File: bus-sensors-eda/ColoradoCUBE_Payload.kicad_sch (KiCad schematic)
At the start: 32 parts, among them J5 Conn_01x02, J6 Conn_01x02, J7 Conn_01x02, SW1 SW_SPST, U1 PIC18F27Q84-E/SP

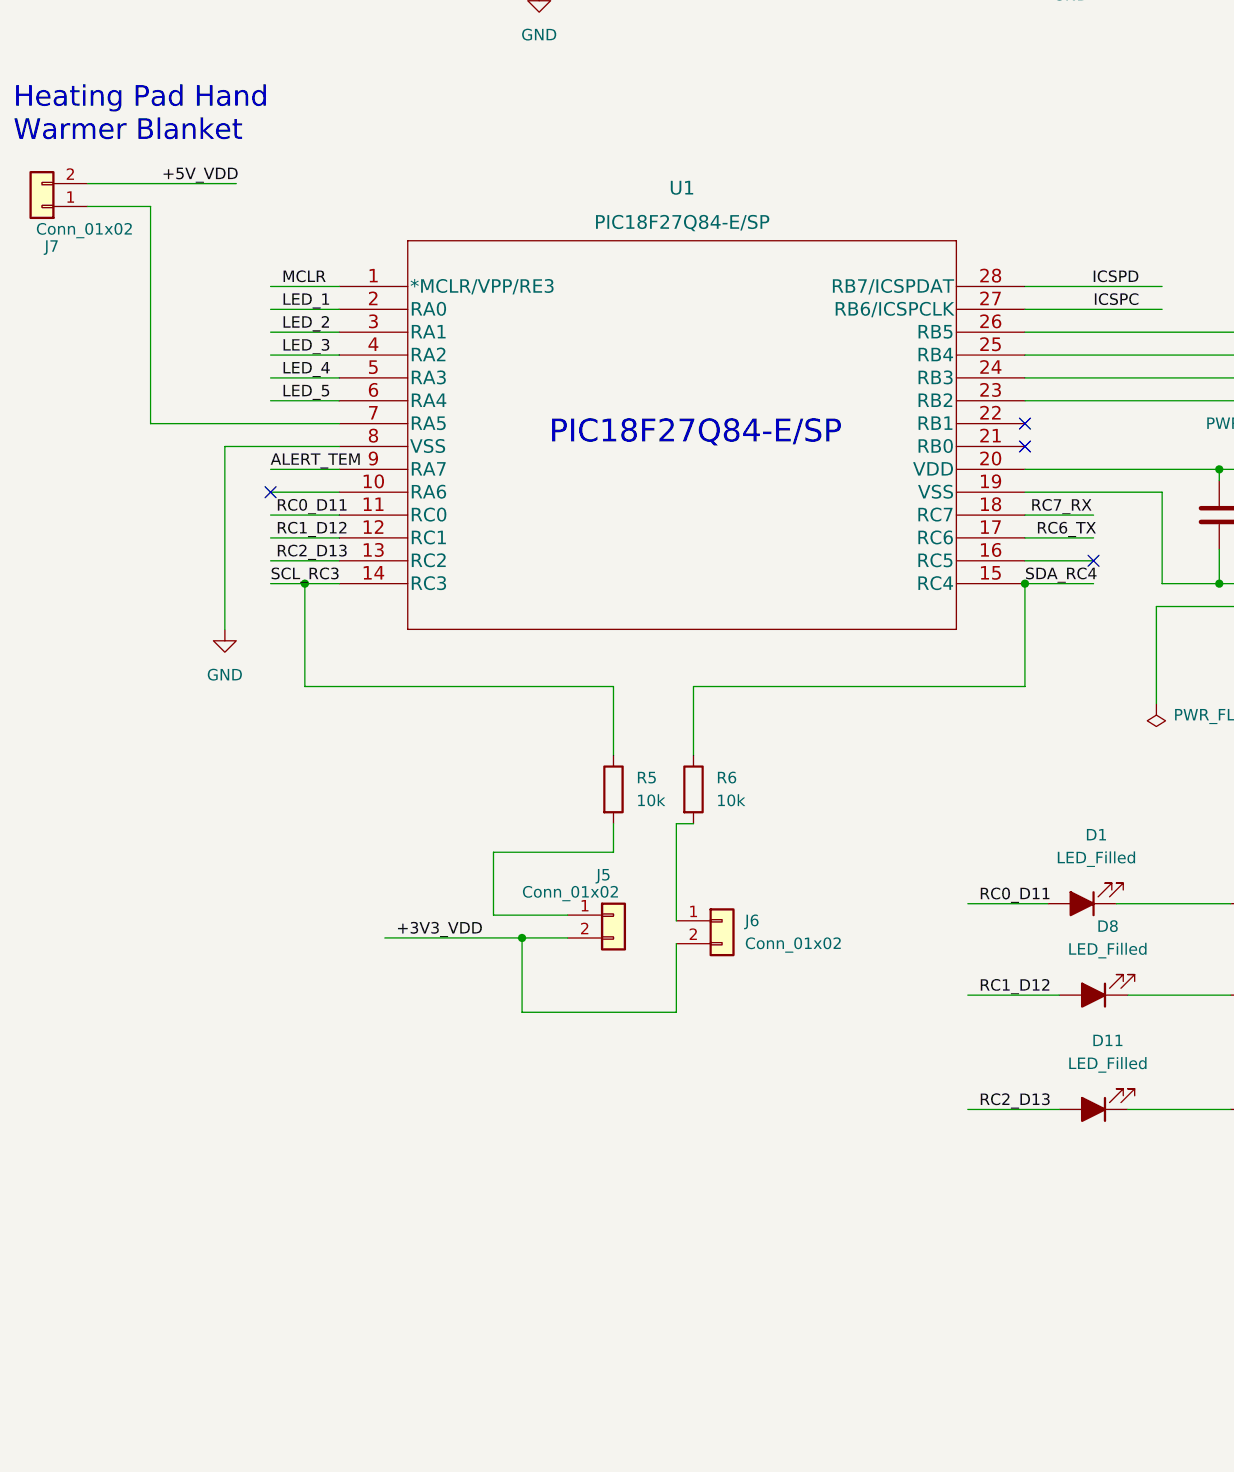
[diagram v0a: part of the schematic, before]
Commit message: moving files under eda dir
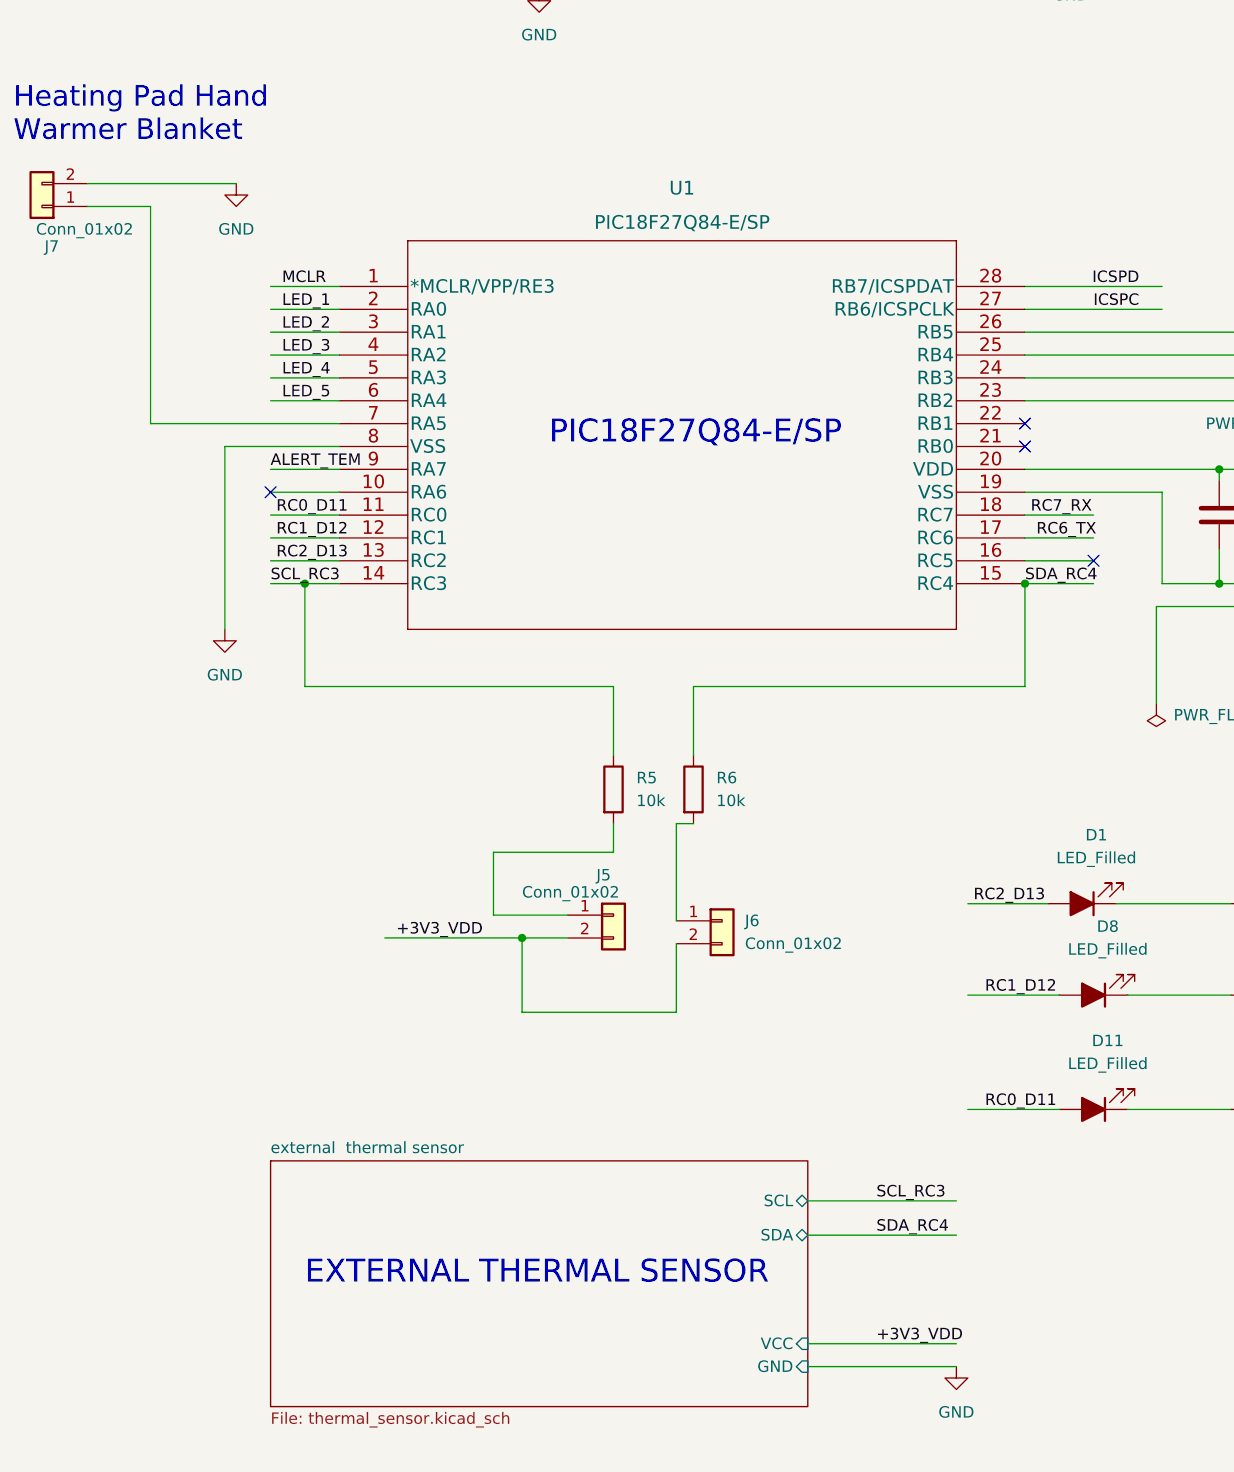
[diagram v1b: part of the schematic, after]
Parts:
- D1, D11, D8: footprint LED_SMD:LED_2512_6332Metric_Pad1.52x3.35mm_HandSolder -> LED_SMD:LED_2010_5025Metric_Pad1.52x2.65mm_HandSolder
- D10, D9: footprint LED_SMD:LED_1210_3225Metric_Pad1.42x2.65mm_HandSolder -> LED_SMD:LED_2010_5025Metric_Pad1.52x2.65mm_HandSolder
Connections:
- net +5V_VDD: no longer J7.2 (Pin_2)
- net GND: now also J7.2 (Pin_2)
- net RC0_D11: now also D11.2 (A); no longer D1.2 (A)
- net RC2_D13: now also D1.2 (A); no longer D11.2 (A)
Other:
- added sheet external  thermal sensor (thermal_sensor.kicad_sch)
- note added: "EXTERNAL THERMAL SENSOR"
